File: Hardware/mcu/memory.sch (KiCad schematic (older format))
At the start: 4 parts, among them U501 AS7C34096A

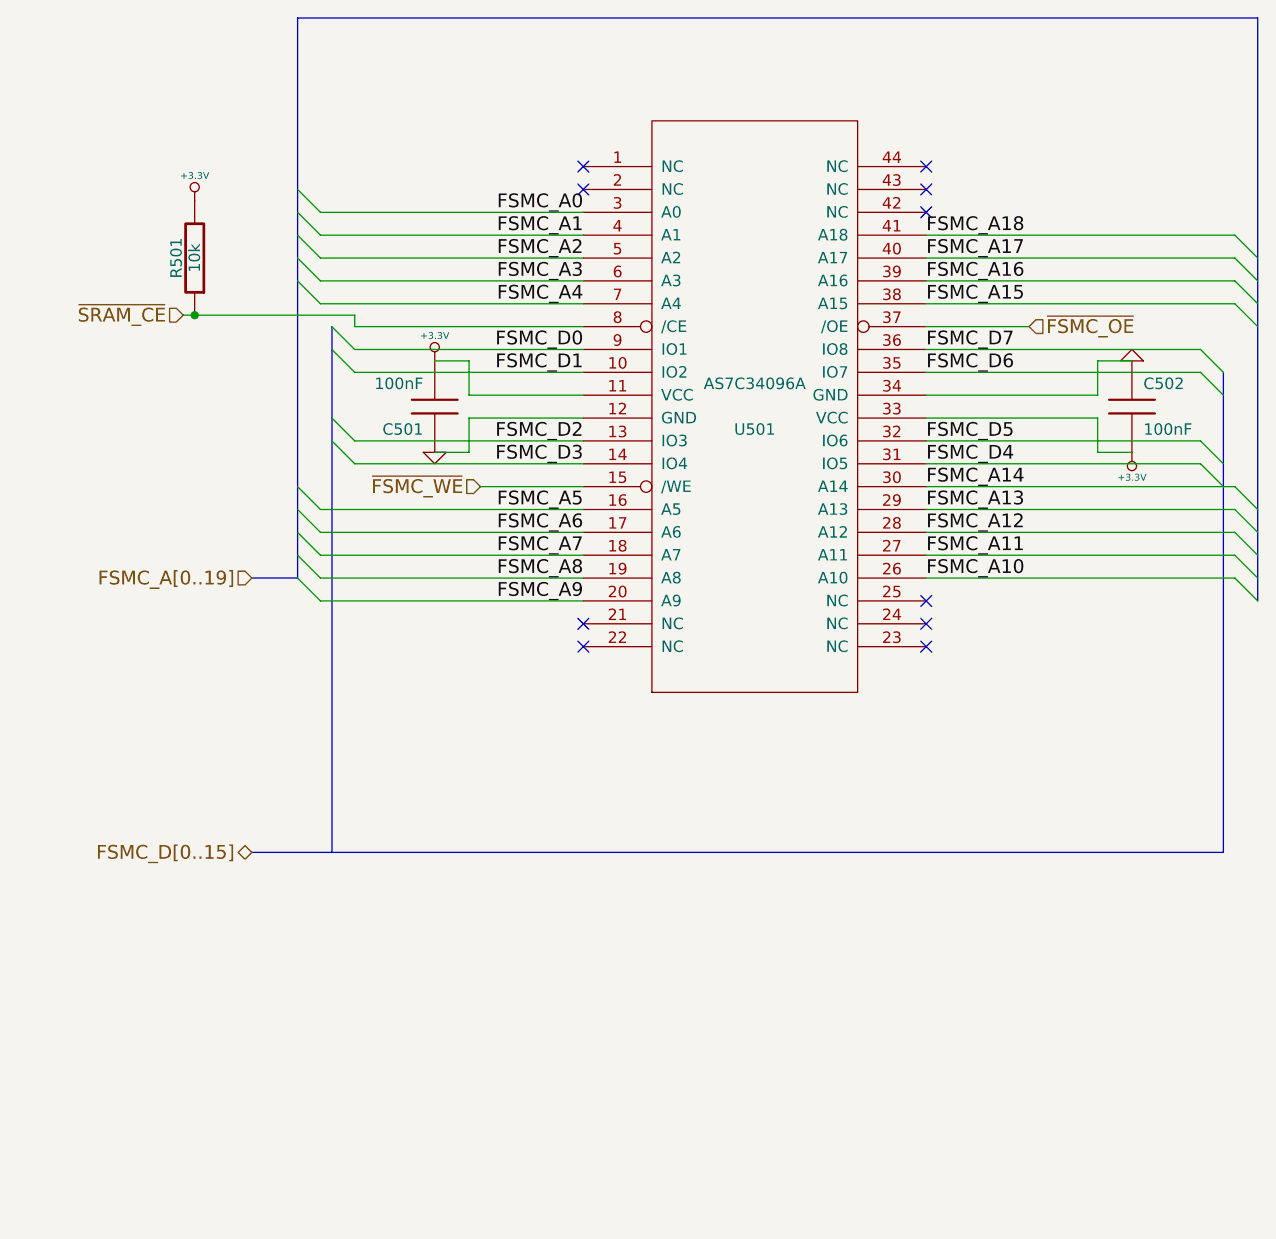
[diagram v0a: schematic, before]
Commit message: splitted schematics are ready. MCU/Display board is ready.
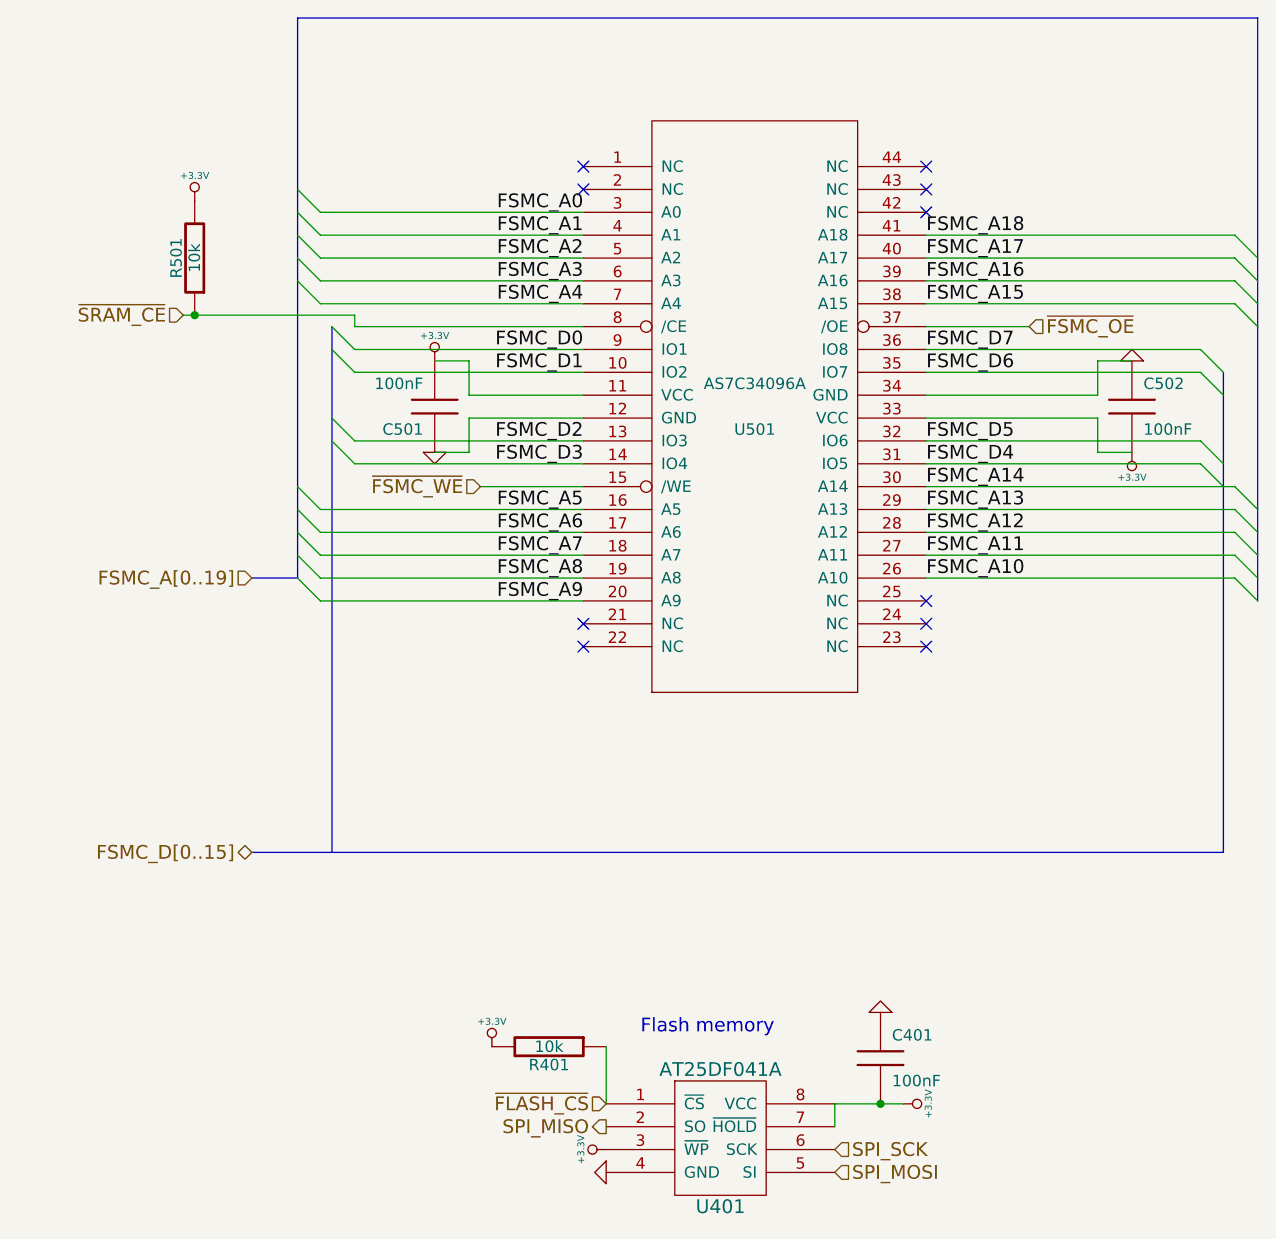
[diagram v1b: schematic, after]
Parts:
- added C401: 100nF, symbol C
- added R401: 10k, symbol R
- added U401: AT25DF041A, symbol AT25DF041A
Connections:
- net +3.3V: now also C401.2, R401.2, U401.3 (~WP), U401.7 (~HOLD), U401.8 (VCC)
- net GND: now also C401.1, U401.4 (GND)
- new net SPI_MISO: U401.2 (SO)
- new net SPI_MOSI: U401.5 (SI)
- new net SPI_SCK: U401.6 (SCK)
- new net ~FLASH_CS: R401.1, U401.1 (~CS)
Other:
- note added: "Flash memory"
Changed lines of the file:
@@
-EESchema Schematic File Version 2  date Do 10 Mär 2011 01:37:58 CET
+EESchema Schematic File Version 2  date Do 10 Mär 2011 16:44:23 CET
 LIBS:power
 LIBS:device
@@
 EELAYER END
 $Descr A4 11700 8267
-Sheet 3 9
+encoding utf-8
+Sheet 4 9
 Title ""
-Date "9 mar 2011"
+Date "10 mar 2011"
 Rev ""
 Comp ""
@@
 $EndDescr
 Wire Wire Line
-	2100 3100 2250 3100
-Wire Wire Line
-	2250 3100 2250 2950
-Wire Wire Line
-	2250 2950 2750 2950
+	2850 5700 2850 5950
+Wire Wire Line
+	3850 6050 3850 5950
+Wire Wire Line
+	2750 2850 2250 2850
+Wire Wire Line
+	2250 2850 2250 2700
+Wire Wire Line
+	2250 2700 2100 2700
+Wire Wire Line
+	4250 2550 4700 2550
+Wire Wire Line
+	1750 2550 1750 2500
+Wire Wire Line
+	1750 2550 2750 2550
+Wire Wire Line
+	5450 3150 4250 3150
+Wire Wire Line
+	5450 2750 4250 2750
+Wire Wire Line
+	2750 3150 1750 3150
+Wire Wire Line
+	2750 2750 1750 2750
+Wire Bus Line
+	5550 2750 5550 4850
+Wire Bus Line
+	1650 4850 1650 2550
+Wire Wire Line
+	4250 2150 5600 2150
+Wire Wire Line
+	4250 2350 5600 2350
+Wire Wire Line
+	4250 3250 5600 3250
+Wire Wire Line
+	4250 3450 5600 3450
+Wire Wire Line
+	4250 3650 5600 3650
+Wire Wire Line
+	2750 2150 1600 2150
+Wire Wire Line
+	2750 2350 1600 2350
+Wire Wire Line
+	1600 3350 2750 3350
+Wire Wire Line
+	1600 3550 2750 3550
+Wire Wire Line
+	1600 3750 2750 3750
+Wire Bus Line
+	1500 1200 5700 1200
+Wire Bus Line
+	1500 1200 1500 3650
+Wire Wire Line
+	4250 2850 5000 2850
+Wire Wire Line
+	5000 2850 5000 2700
+Wire Wire Line
+	5000 2700 5150 2700
+Wire Wire Line
+	4250 2950 5000 2950
+Wire Wire Line
+	5000 2950 5000 3100
+Wire Wire Line
+	5000 3100 5150 3100
+Wire Bus Line
+	5700 1200 5700 3750
+Wire Wire Line
+	2750 3650 1600 3650
+Wire Wire Line
+	2750 3450 1600 3450
+Wire Wire Line
+	1600 2450 2750 2450
+Wire Wire Line
+	1600 2250 2750 2250
+Wire Wire Line
+	1600 2050 2750 2050
+Wire Wire Line
+	5600 3550 4250 3550
+Wire Wire Line
+	5600 3350 4250 3350
+Wire Wire Line
+	5600 2450 4250 2450
+Wire Wire Line
+	5600 2250 4250 2250
+Wire Bus Line
+	1500 3650 1300 3650
+Wire Wire Line
+	1750 2650 2750 2650
+Wire Wire Line
+	1750 3050 2750 3050
+Wire Wire Line
+	4250 2650 5450 2650
+Wire Wire Line
+	4250 3050 5450 3050
+Wire Bus Line
+	5550 4850 1300 4850
+Wire Wire Line
+	1750 2500 1000 2500
+Connection ~ 1050 2500
 Wire Wire Line
 	2300 3250 2750 3250
-Connection ~ 1050 2500
-Wire Wire Line
-	1000 2500 1750 2500
-Wire Bus Line
-	1300 4850 5550 4850
-Wire Wire Line
-	4250 3050 5450 3050
-Wire Wire Line
-	4250 2650 5450 2650
-Wire Wire Line
-	1750 3050 2750 3050
-Wire Wire Line
-	1750 2650 2750 2650
-Wire Bus Line
-	1300 3650 1500 3650
-Wire Wire Line
-	5600 2250 4250 2250
-Wire Wire Line
-	5600 2450 4250 2450
-Wire Wire Line
-	5600 3350 4250 3350
-Wire Wire Line
-	5600 3550 4250 3550
-Wire Wire Line
-	1600 2050 2750 2050
-Wire Wire Line
-	1600 2250 2750 2250
-Wire Wire Line
-	1600 2450 2750 2450
-Wire Wire Line
-	2750 3450 1600 3450
-Wire Wire Line
-	2750 3650 1600 3650
-Wire Bus Line
-	5700 3750 5700 1200
-Wire Wire Line
-	5150 3100 5000 3100
-Wire Wire Line
-	5000 3100 5000 2950
-Wire Wire Line
-	5000 2950 4250 2950
-Wire Wire Line
-	5150 2700 5000 2700
-Wire Wire Line
-	5000 2700 5000 2850
-Wire Wire Line
-	5000 2850 4250 2850
-Wire Bus Line
-	1500 3650 1500 1200
-Wire Bus Line
-	1500 1200 5700 1200
-Wire Wire Line
-	1600 3750 2750 3750
-Wire Wire Line
-	1600 3550 2750 3550
-Wire Wire Line
-	1600 3350 2750 3350
-Wire Wire Line
-	2750 2350 1600 2350
-Wire Wire Line
-	2750 2150 1600 2150
-Wire Wire Line
-	4250 3650 5600 3650
-Wire Wire Line
-	4250 3450 5600 3450
-Wire Wire Line
-	4250 3250 5600 3250
-Wire Wire Line
-	4250 2350 5600 2350
-Wire Wire Line
-	4250 2150 5600 2150
-Wire Bus Line
-	1650 4850 1650 2550
-Wire Bus Line
-	5550 4850 5550 2750
-Wire Wire Line
-	2750 2750 1750 2750
-Wire Wire Line
-	2750 3150 1750 3150
-Wire Wire Line
-	5450 2750 4250 2750
-Wire Wire Line
-	5450 3150 4250 3150
-Wire Wire Line
-	2750 2550 1750 2550
-Wire Wire Line
-	1750 2550 1750 2500
-Wire Wire Line
-	4250 2550 4700 2550
-Wire Wire Line
-	2100 2700 2250 2700
-Wire Wire Line
-	2250 2700 2250 2850
-Wire Wire Line
-	2250 2850 2750 2850
-$Comp
-L GND #PWR07
+Wire Wire Line
+	2750 2950 2250 2950
+Wire Wire Line
+	2250 2950 2250 3100
+Wire Wire Line
+	2250 3100 2100 3100
+Wire Wire Line
+	3850 5950 4150 5950
+Connection ~ 4050 5950
+$Comp
+L +3.3V #PWR404
+U 1 1 4D78F1D0
+P 2350 5700
+F 0 "#PWR404" H 2350 5660 30  0001 C CNN
+F 1 "+3.3V" H 2350 5810 30  0000 C CNN
+	1    2350 5700
+	1    0    0    -1
+$EndComp
+$Comp
+L R R401
+U 1 1 4D78F1C7
+P 2600 5700
+F 0 "R401" V 2680 5700 50  0000 C CNN
+F 1 "10k" V 2600 5700 50  0000 C CNN
+	1    2600 5700
+	0    1    1    0
+$EndComp
+$Comp
+L GND #PWR406
+U 1 1 4D78ED01
+P 2850 6250
+F 0 "#PWR406" H 2850 6250 30  0001 C CNN
+F 1 "GND" H 2850 6180 30  0001 C CNN
+	1    2850 6250
+	0    1    1    0
+$EndComp
+$Comp
+L +3.3V #PWR405
+U 1 1 4D78ECF8
+P 2850 6150
+F 0 "#PWR405" H 2850 6110 30  0001 C CNN
+F 1 "+3.3V" H 2850 6260 30  0000 C CNN
+	1    2850 6150
+	0    -1   -1   0
+$EndComp
+Text HLabel 3850 6150 2    60   Input ~ 0
+SPI_SCK
+Text HLabel 3850 6250 2    60   Input ~ 0
+SPI_MOSI
+Text HLabel 2850 6050 0    60   Output ~ 0
+SPI_MISO
+Text HLabel 2850 5950 0    60   Input ~ 0
+~FLASH_CS
+$Comp
+L +3.3V #PWR408
+U 1 1 4D78ECB1
+P 4150 5950
+F 0 "#PWR408" H 4150 5910 30  0001 C CNN
+F 1 "+3.3V" H 4150 6060 30  0000 C CNN
+	1    4150 5950
+	0    1    1    0
+$EndComp
+$Comp
+L GND #PWR407
+U 1 1 4D78ECAD
+P 4050 5550
+F 0 "#PWR407" H 4050 5550 30  0001 C CNN
+F 1 "GND" H 4050 5480 30  0001 C CNN
+	1    4050 5550
+	-1   0    0    1
+$EndComp
+$Comp
+L C C401
+U 1 1 4D78ECA8
+P 4050 5750
+F 0 "C401" H 4100 5850 50  0000 L CNN
+F 1 "100nF" H 4100 5650 50  0000 L CNN
+	1    4050 5750
+	1    0    0    -1
+$EndComp
+Text Notes 3000 5650 0    60   ~ 0
+Flash memory
+$Comp
+L AT25DF041A U401
+U 1 1 4D78ECA0
+P 3350 6100
+F 0 "U401" H 3350 5800 60  0000 C CNN
+F 1 "AT25DF041A" H 3350 6400 60  0000 C CNN
+	1    3350 6100
+	1    0    0    -1
+$EndComp
+$Comp
+L GND #PWR403
 U 1 1 4D744D91
 P 2100 3100
-F 0 "#PWR07" H 2100 3100 30  0001 C CNN
+F 0 "#PWR403" H 2100 3100 30  0001 C CNN
 F 1 "GND" H 2100 3030 30  0001 C CNN
 	1    2100 3100
@@
 $EndComp
 $Comp
-L +3.3V #PWR08
+L +3.3V #PWR402
 U 1 1 4D744D8F
 P 2100 2700
-F 0 "#PWR08" H 2100 2660 30  0001 C CNN
+F 0 "#PWR402" H 2100 2660 30  0001 C CNN
 F 1 "+3.3V" H 2100 2810 30  0000 C CNN
 	1    2100 2700
@@
 ~SRAM_CE
 $Comp
-L +3.3V #PWR09
+L +3.3V #PWR401
 U 1 1 4D744D1A
 P 1050 2000
-F 0 "#PWR09" H 1050 1960 30  0001 C CNN
+F 0 "#PWR401" H 1050 1960 30  0001 C CNN
 F 1 "+3.3V" H 1050 2110 30  0000 C CNN
 	1    1050 2000
@@
 	1500 3650 1600 3750
 $Comp
-L +3.3V #PWR010
+L +3.3V #PWR410
 U 1 1 4D744A4B
 P 5150 3100
-F 0 "#PWR010" H 5150 3060 30  0001 C CNN
+F 0 "#PWR410" H 5150 3060 30  0001 C CNN
 F 1 "+3.3V" H 5150 3210 30  0000 C CNN
 	1    5150 3100
@@
 $EndComp
 $Comp
-L GND #PWR011
+L GND #PWR409
 U 1 1 4D744A44
 P 5150 2700
-F 0 "#PWR011" H 5150 2700 30  0001 C CNN
+F 0 "#PWR409" H 5150 2700 30  0001 C CNN
 F 1 "GND" H 5150 2630 30  0001 C CNN
 	1    5150 2700
